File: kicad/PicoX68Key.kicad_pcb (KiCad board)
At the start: 2 copper layers, 33.9 x 69 mm, 22 parts, among them J1 LED_BOARD, J2 MINI-DIN-7, Q1 2N7000, Q2 2N7000, Q3 2N7000, U1 Pico

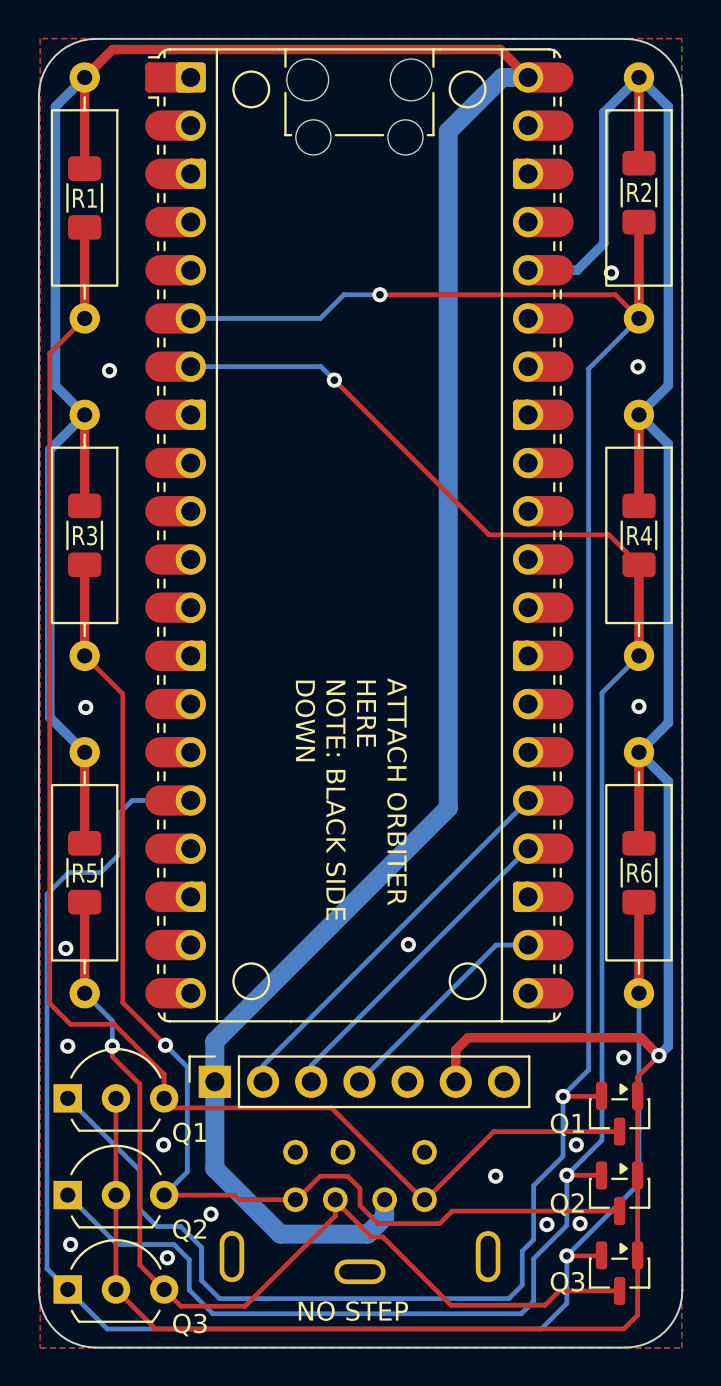
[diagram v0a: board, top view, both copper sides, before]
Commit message: Fixed B2B interconnect clearance
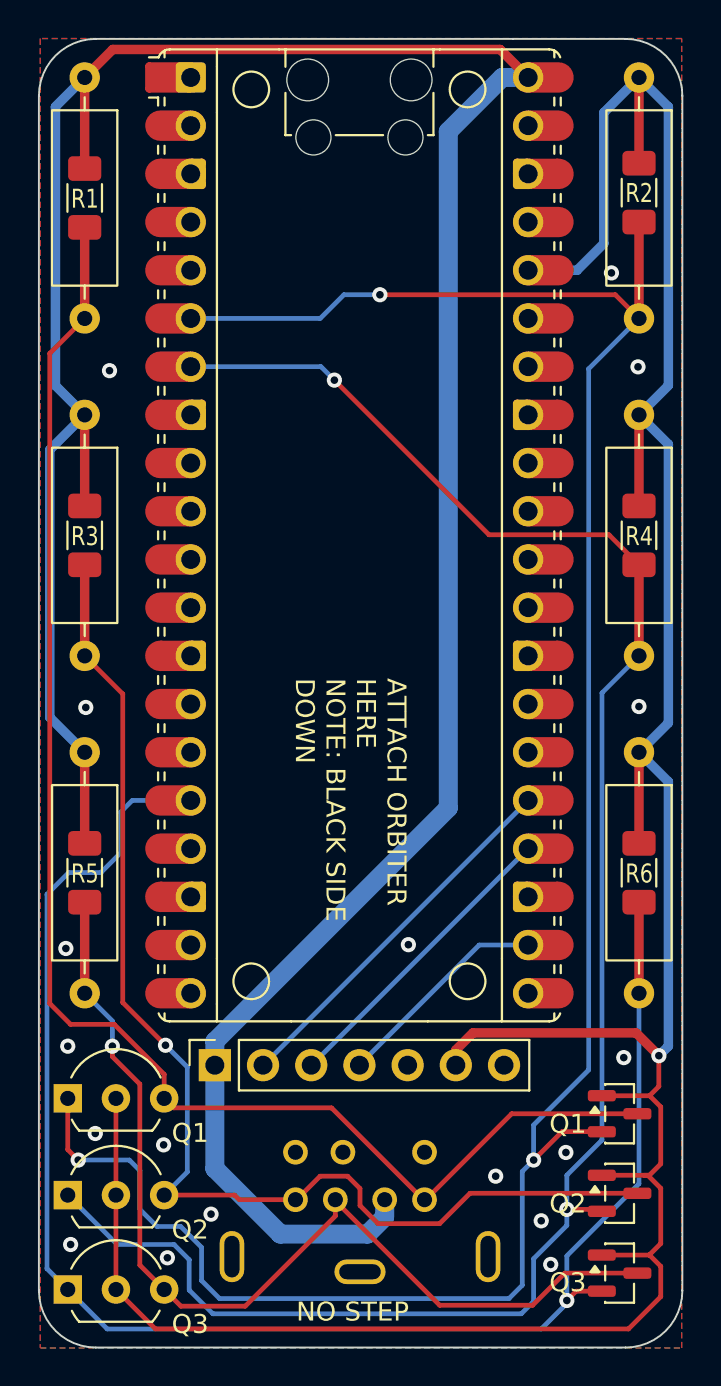
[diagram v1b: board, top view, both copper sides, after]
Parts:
- moved J1 0.88 mm to (76.2, 134.6)
- turned SQ1 to 0 degrees
- turned SQ2 to 0 degrees
- turned SQ3 to 0 degrees
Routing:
- net 3V3: track 149.1 -> 157.9 mm
- net KB_TX_L: track 116.3 -> 120.1 mm, vias 2 -> 3
- net MS_TX_H: track 51.9 -> 53.2 mm
- net KB_RX_H: track 62.9 -> 64.2 mm
- net KB_TX_H: track 78.3 -> 79.6 mm
- net SCL: track 17.0 -> 16.2 mm
- net MOSI: track 20.6 -> 19.7 mm
- net GND: vias 17 -> 18
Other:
- board text added: "CS"
- board text removed: "L_EN"

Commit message: Add PWM functionality to set LED brightness
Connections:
- J1 pad 5: unconnected-(J1-Pin_5-Pad5) -> OE
- U1 pad 21: unconnected-(U1-GPIO16-Pad21)_1 -> OE
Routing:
- net OE: track 0.00 -> 7.92 mm
- net GND: vias 18 -> 19
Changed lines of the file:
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@@
 	(net 8 "KB_RX_L")
 	(net 9 "MS_TX_L")
-	(net 10 "unconnected-(J1-Pin_5-Pad5)")
+	(net 10 "OE")
 	(net 11 "SCL")
 	(net 12 "unconnected-(U1-GPIO9-Pad12)")
@@
 	(net 30 "unconnected-(J2-Pad6)")
 	(net 31 "unconnected-(U1-RUN-Pad30)_1")
-	(net 32 "unconnected-(U1-GPIO16-Pad21)_1")
+	(net 32 "unconnected-(U1-RUN-Pad30)")
 	(net 33 "unconnected-(U1-GPIO28_ADC2-Pad34)_1")
 	(net 34 "unconnected-(U1-GPIO7-Pad10)_1")
@@
 	(net 38 "unconnected-(U1-ADC_VREF-Pad35)_1")
 	(net 39 "unconnected-(U1-GPIO26_ADC0-Pad31)_1")
+	(net 40 "unconnected-(U1-GPIO26_ADC0-Pad31)")
+	(net 41 "unconnected-(U1-ADC_VREF-Pad35)")
+	(net 42 "unconnected-(U1-GPIO3-Pad5)")
+	(net 43 "unconnected-(U1-GPIO28_ADC2-Pad34)")
+	(net 44 "unconnected-(U1-VSYS-Pad39)_1")
+	(net 45 "unconnected-(U1-GPIO7-Pad10)")
+	(net 46 "unconnected-(U1-GPIO21-Pad27)_1")
+	(net 47 "unconnected-(U1-GPIO20-Pad26)_1")
+	(net 48 "unconnected-(U1-GPIO13-Pad17)")
+	(net 49 "unconnected-(U1-GPIO15-Pad20)")
+	(net 50 "unconnected-(U1-GPIO10-Pad14)_1")
+	(net 51 "unconnected-(U1-GPIO27_ADC1-Pad32)_1")
+	(net 52 "unconnected-(U1-GPIO2-Pad4)_1")
+	(net 53 "unconnected-(U1-GPIO11-Pad15)_1")
+	(net 54 "unconnected-(U1-GPIO1-Pad2)_1")
+	(net 55 "unconnected-(U1-GPIO6-Pad9)_1")
+	(net 56 "unconnected-(U1-3V3_EN-Pad37)_1")
+	(net 57 "unconnected-(U1-GPIO9-Pad12)_1")
+	(net 58 "unconnected-(U1-GPIO14-Pad19)_1")
+	(net 59 "unconnected-(U1-GPIO22-Pad29)_1")
+	(net 60 "unconnected-(U1-GPIO8-Pad11)_1")
+	(net 61 "unconnected-(U1-GPIO0-Pad1)_1")
 	(footprint "Package_TO_SOT_THT:TO-92L_Inline_Wide"
 		(layer "F.Cu")
@@
 			(remove_unused_layers no)
 			(roundrect_rratio 0.125)
-			(net 28 "unconnected-(U1-GPIO0-Pad1)")
+			(net 61 "unconnected-(U1-GPIO0-Pad1)_1")
 			(pinfunction "GPIO0")
 			(pintype "bidirectional+no_connect")
@@
 			(layers "F.Cu" "F.Mask")
 			(roundrect_rratio 0.5)
-			(net 14 "unconnected-(U1-GPIO1-Pad2)")
+			(net 54 "unconnected-(U1-GPIO1-Pad2)_1")
 			(pinfunction "GPIO1")
 			(pintype "bidirectional+no_connect")
@@
 			(layers "F.Cu" "F.Mask")
 			(roundrect_rratio 0.5)
-			(net 22 "unconnected-(U1-GPIO2-Pad4)")
+			(net 52 "unconnected-(U1-GPIO2-Pad4)_1")
 			(pinfunction "GPIO2")
 			(pintype "bidirectional+no_connect")
@@
 			(layers "F.Cu" "F.Mask")
 			(roundrect_rratio 0.5)
-			(net 37 "unconnected-(U1-GPIO3-Pad5)_1")
+			(net 42 "unconnected-(U1-GPIO3-Pad5)")
 			(pinfunction "GPIO3")
 			(pintype "bidirectional+no_connect")
@@
 			(layers "*.Cu" "*.Mask")
 			(remove_unused_layers no)
-			(net 24 "unconnected-(U1-GPIO6-Pad9)")
+			(net 55 "unconnected-(U1-GPIO6-Pad9)_1")
 			(pinfunction "GPIO6")
 			(pintype "bidirectional+no_connect")
@@
 			(layers "*.Cu" "*.Mask")
 			(remove_unused_layers no)
-			(net 34 "unconnected-(U1-GPIO7-Pad10)_1")
+			(net 45 "unconnected-(U1-GPIO7-Pad10)")
 			(pinfunction "GPIO7")
 			(pintype "bidirectional+no_connect")
@@
 			(layers "*.Cu" "*.Mask")
 			(remove_unused_layers no)
-			(net 27 "unconnected-(U1-GPIO8-Pad11)")
+			(net 60 "unconnected-(U1-GPIO8-Pad11)_1")
 			(pinfunction "GPIO8")
 			(pintype "bidirectional+no_connect")
@@
 			(layers "F.Cu" "F.Mask")
 			(roundrect_rratio 0.5)
-			(net 12 "unconnected-(U1-GPIO9-Pad12)")
+			(net 57 "unconnected-(U1-GPIO9-Pad12)_1")
 			(pinfunction "GPIO9")
 			(pintype "bidirectional+no_connect")
@@
 			(layers "*.Cu" "*.Mask")
 			(remove_unused_layers no)
-			(net 21 "unconnected-(U1-GPIO10-Pad14)")
+			(net 50 "unconnected-(U1-GPIO10-Pad14)_1")
 			(pinfunction "GPIO10")
 			(pintype "bidirectional+no_connect")
@@
 			(layers "*.Cu" "*.Mask")
 			(remove_unused_layers no)
-			(net 23 "unconnected-(U1-GPIO11-Pad15)")
+			(net 53 "unconnected-(U1-GPIO11-Pad15)_1")
 			(pinfunction "GPIO11")
 			(pintype "bidirectional+no_connect")
@@
 			(layers "*.Cu" "*.Mask")
 			(remove_unused_layers no)
-			(net 35 "unconnected-(U1-GPIO13-Pad17)_1")
+			(net 48 "unconnected-(U1-GPIO13-Pad17)")
 			(pinfunction "GPIO13")
 			(pintype "bidirectional+no_connect")
@@
 			(layers "F.Cu" "F.Mask")
 			(roundrect_rratio 0.5)
-			(net 17 "unconnected-(U1-GPIO14-Pad19)")
+			(net 58 "unconnected-(U1-GPIO14-Pad19)_1")
 			(pinfunction "GPIO14")
 			(pintype "bidirectional+no_connect")
@@
 			(layers "F.Cu" "F.Mask")
 			(roundrect_rratio 0.5)
-			(net 36 "unconnected-(U1-GPIO15-Pad20)_1")
+			(net 49 "unconnected-(U1-GPIO15-Pad20)")
 			(pinfunction "GPIO15")
 			(pintype "bidirectional+no_connect")
@@
 			(layers "*.Cu" "*.Mask")
 			(remove_unused_layers no)
-			(net 32 "unconnected-(U1-GPIO16-Pad21)_1")
+			(net 10 "OE")
 			(pinfunction "GPIO16")
-			(pintype "bidirectional+no_connect")
+			(pintype "bidirectional")
 		)
 		(pad "21" smd roundrect
@@
 			(layers "F.Cu" "F.Mask")
 			(roundrect_rratio 0.5)
-			(net 32 "unconnected-(U1-GPIO16-Pad21)_1")
+			(net 10 "OE")
 			(pinfunction "GPIO16")
-			(pintype "bidirectional+no_connect")
+			(pintype "bidirectional")
 		)
 		(pad "22" thru_hole circle
@@
 			(layers "*.Cu" "*.Mask")
 			(remove_unused_layers no)
-			(net 18 "unconnected-(U1-GPIO20-Pad26)")
+			(net 47 "unconnected-(U1-GPIO20-Pad26)_1")
 			(pinfunction "GPIO20")
 			(pintype "bidirectional+no_connect")
@@
 			(layers "F.Cu" "F.Mask")
 			(roundrect_rratio 0.5)
-			(net 15 "unconnected-(U1-GPIO21-Pad27)")
+			(net 46 "unconnected-(U1-GPIO21-Pad27)_1")
 			(pinfunction "GPIO21")
 			(pintype "bidirectional+no_connect")
@@
 			(layers "*.Cu" "*.Mask")
 			(remove_unused_layers no)
-			(net 26 "unconnected-(U1-GPIO22-Pad29)")
+			(net 59 "unconnected-(U1-GPIO22-Pad29)_1")
 			(pinfunction "GPIO22")
 			(pintype "bidirectional+no_connect")
@@
 			(layers "*.Cu" "*.Mask")
 			(remove_unused_layers no)
-			(net 31 "unconnected-(U1-RUN-Pad30)_1")
+			(net 32 "unconnected-(U1-RUN-Pad30)")
 			(pinfunction "RUN")
 			(pintype "input+no_connect")
@@
 			(layers "F.Cu" "F.Mask")
 			(roundrect_rratio 0.5)
-			(net 39 "unconnected-(U1-GPIO26_ADC0-Pad31)_1")
+			(net 40 "unconnected-(U1-GPIO26_ADC0-Pad31)")
 			(pinfunction "GPIO26_ADC0")
 			(pintype "bidirectional+no_connect")
@@
 			(layers "F.Cu" "F.Mask")
 			(roundrect_rratio 0.5)
-			(net 19 "unconnected-(U1-GPIO27_ADC1-Pad32)")
+			(net 51 "unconnected-(U1-GPIO27_ADC1-Pad32)_1")
 			(pinfunction "GPIO27_ADC1")
 			(pintype "bidirectional+no_connect")
@@
 			(layers "*.Cu" "*.Mask")
 			(remove_unused_layers no)
-			(net 33 "unconnected-(U1-GPIO28_ADC2-Pad34)_1")
+			(net 43 "unconnected-(U1-GPIO28_ADC2-Pad34)")
 			(pinfunction "GPIO28_ADC2")
 			(pintype "bidirectional+no_connect")
@@
 			(layers "F.Cu" "F.Mask")
 			(roundrect_rratio 0.5)
-			(net 38 "unconnected-(U1-ADC_VREF-Pad35)_1")
+			(net 41 "unconnected-(U1-ADC_VREF-Pad35)")
 			(pinfunction "ADC_VREF")
 			(pintype "power_in+no_connect")
@@
 			(layers "*.Cu" "*.Mask")
 			(remove_unused_layers no)
-			(net 25 "unconnected-(U1-3V3_EN-Pad37)")
+			(net 56 "unconnected-(U1-3V3_EN-Pad37)_1")
 			(pinfunction "3V3_EN")
 			(pintype "input+no_connect")
@@
 			(layers "F.Cu" "F.Mask")
 			(roundrect_rratio 0.5)
-			(net 16 "unconnected-(U1-VSYS-Pad39)")
+			(net 44 "unconnected-(U1-VSYS-Pad39)_1")
 			(pinfunction "VSYS")
 			(pintype "power_in+no_connect")
@@
 			(layers "*.Cu" "*.Mask")
 			(remove_unused_layers no)
-			(net 10 "unconnected-(J1-Pin_5-Pad5)")
+			(net 10 "OE")
 			(pinfunction "Pin_5")
-			(pintype "passive+no_connect")
+			(pintype "passive")
 		)
 		(pad "6" thru_hole circle
@@
 	)
 	(via
+		(at 90.25 129.55)
+		(size 0.8)
+		(drill 0.4)
+		(layers "F.Cu" "B.Cu")
+		(free yes)
+		(net 5)
+	)
+	(via
 		(at 70.65 98)
 		(size 0.8)
@@
 	)
 	(segment
+		(start 92.71 130.81)
+		(end 90.15 130.81)
+		(width 0.25)
+		(layer "B.Cu")
+		(net 10)
+	)
+	(segment
+		(start 90.15 130.81)
+		(end 86.36 134.6)
+		(width 0.25)
+		(layer "B.Cu")
+		(net 10)
+	)
+	(segment

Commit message: Add label for OE/PWM pin on interconnect
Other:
- board text added: "OE"
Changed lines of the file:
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@@
+		)
+	)
+	(gr_text "OE"
+		(at 87.05 133.5 90)
+		(layer "B.SilkS")
+		(effects
+			(font
+				(size 1 1)
+				(thickness 0.15)
+			)
+			(justify right bottom mirror)
 		)
 	)

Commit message: Updated credits
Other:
- board text added: "Designed by RetroSwim Thanks to Zuofo, Guddler, tmk, P.Smart"
- board text removed: "Designed by RetroSwim Thanks to Zuofo, Guddler, tmk"
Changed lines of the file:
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@@
 		)
 	)
-	(gr_text "Designed by RetroSwim\nThanks to Zuofo, Guddler, tmk"
+	(gr_text "Designed by RetroSwim\nThanks to Zuofo, Guddler, tmk, P.Smart"
 		(at 97.25 86.4 90)
 		(layer "B.SilkS")

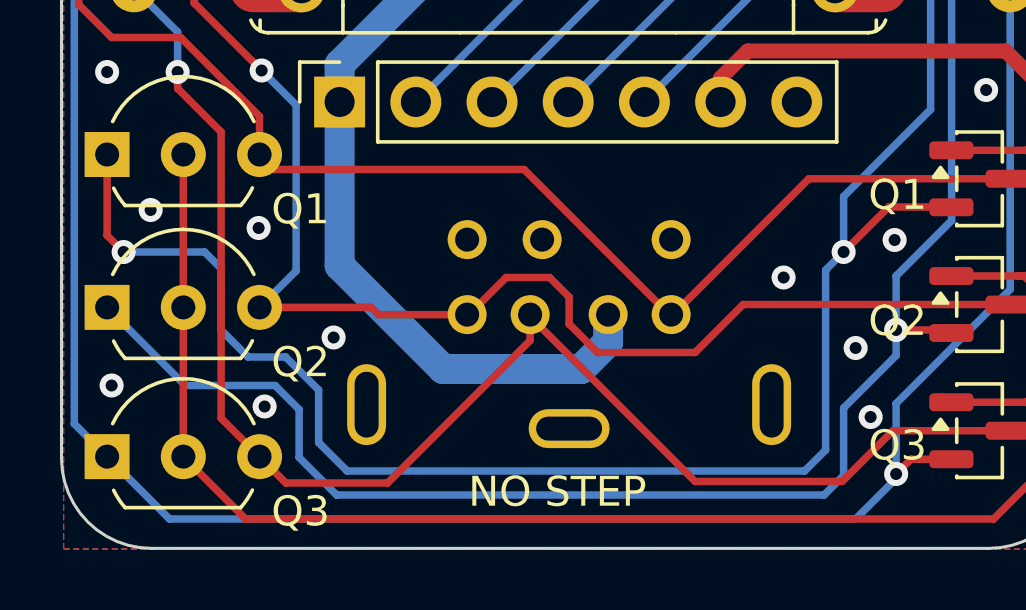
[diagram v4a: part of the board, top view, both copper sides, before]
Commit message: Changes to enable brightness control. Final PCB polish.
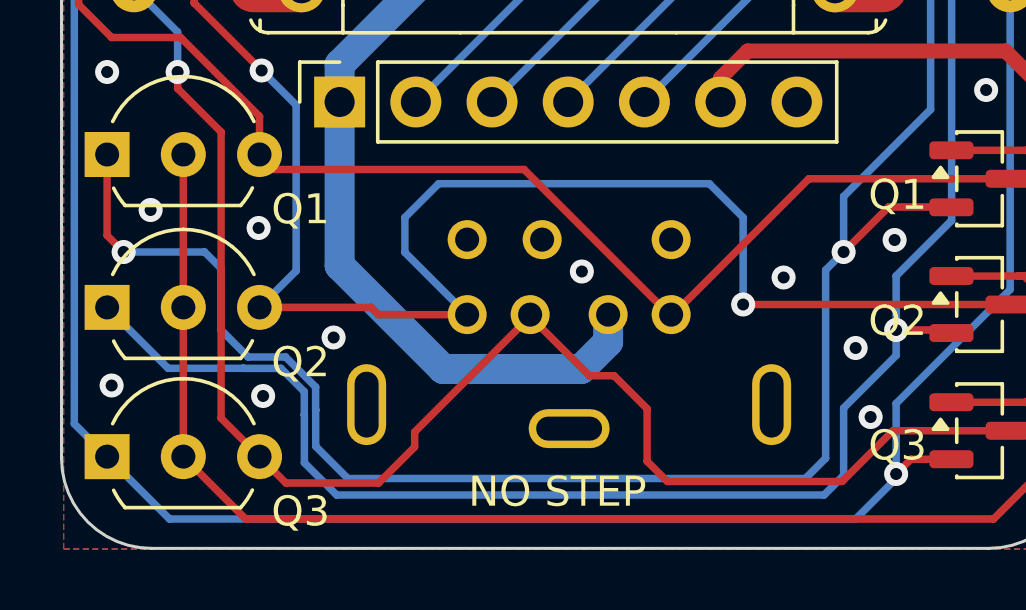
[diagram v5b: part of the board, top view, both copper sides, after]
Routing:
- net KB_RX_H: track 64.2 -> 71.4 mm, vias 1 -> 2
- net MS_TX_H: track 53.2 -> 54.1 mm
- net GND: vias 19 -> 20
